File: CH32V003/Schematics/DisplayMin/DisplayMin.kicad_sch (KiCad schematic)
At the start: 9 parts

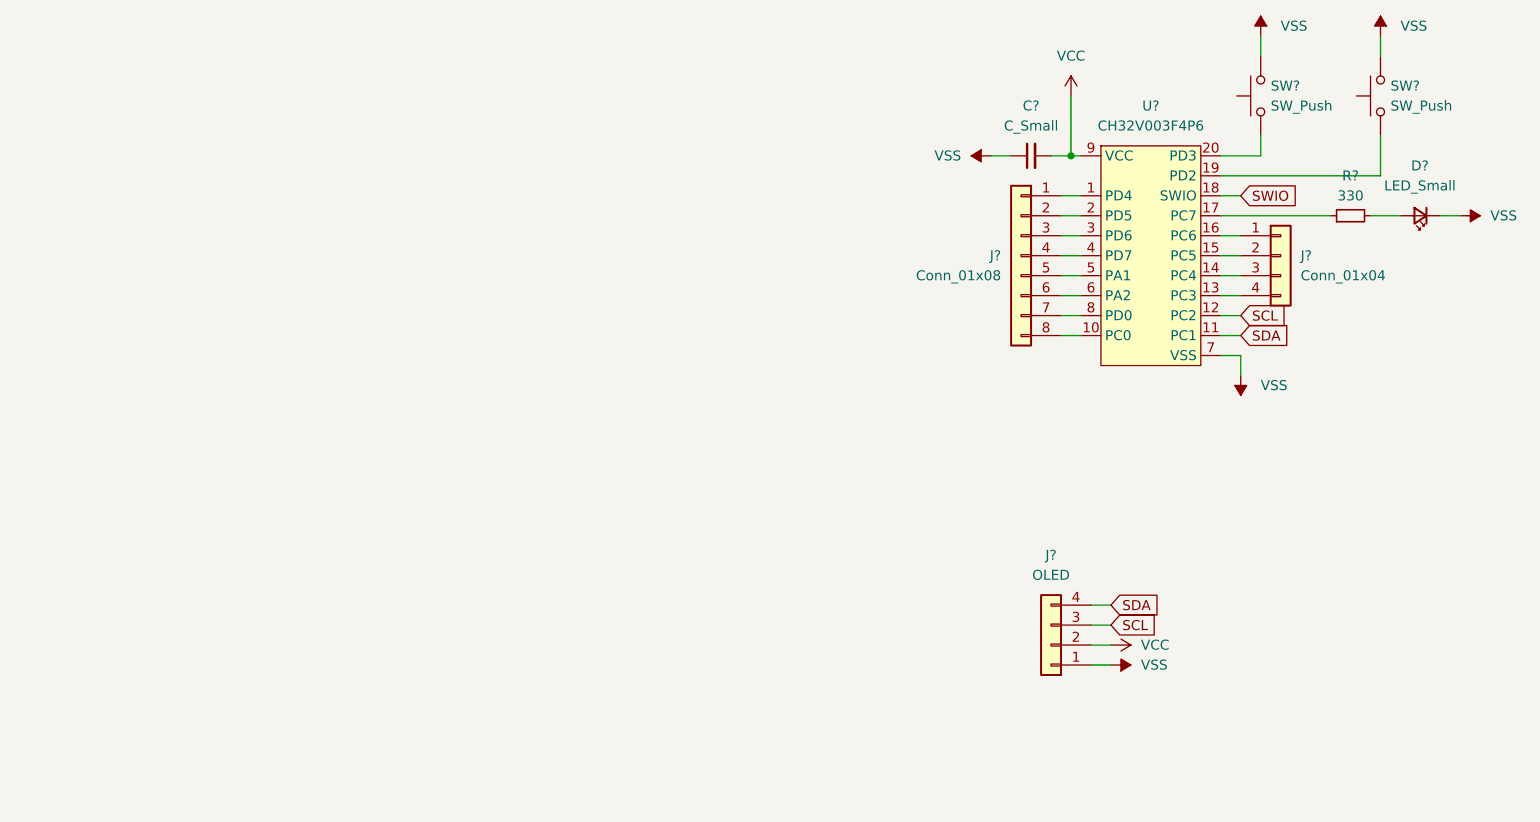
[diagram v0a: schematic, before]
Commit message: 003 dev board with display closer
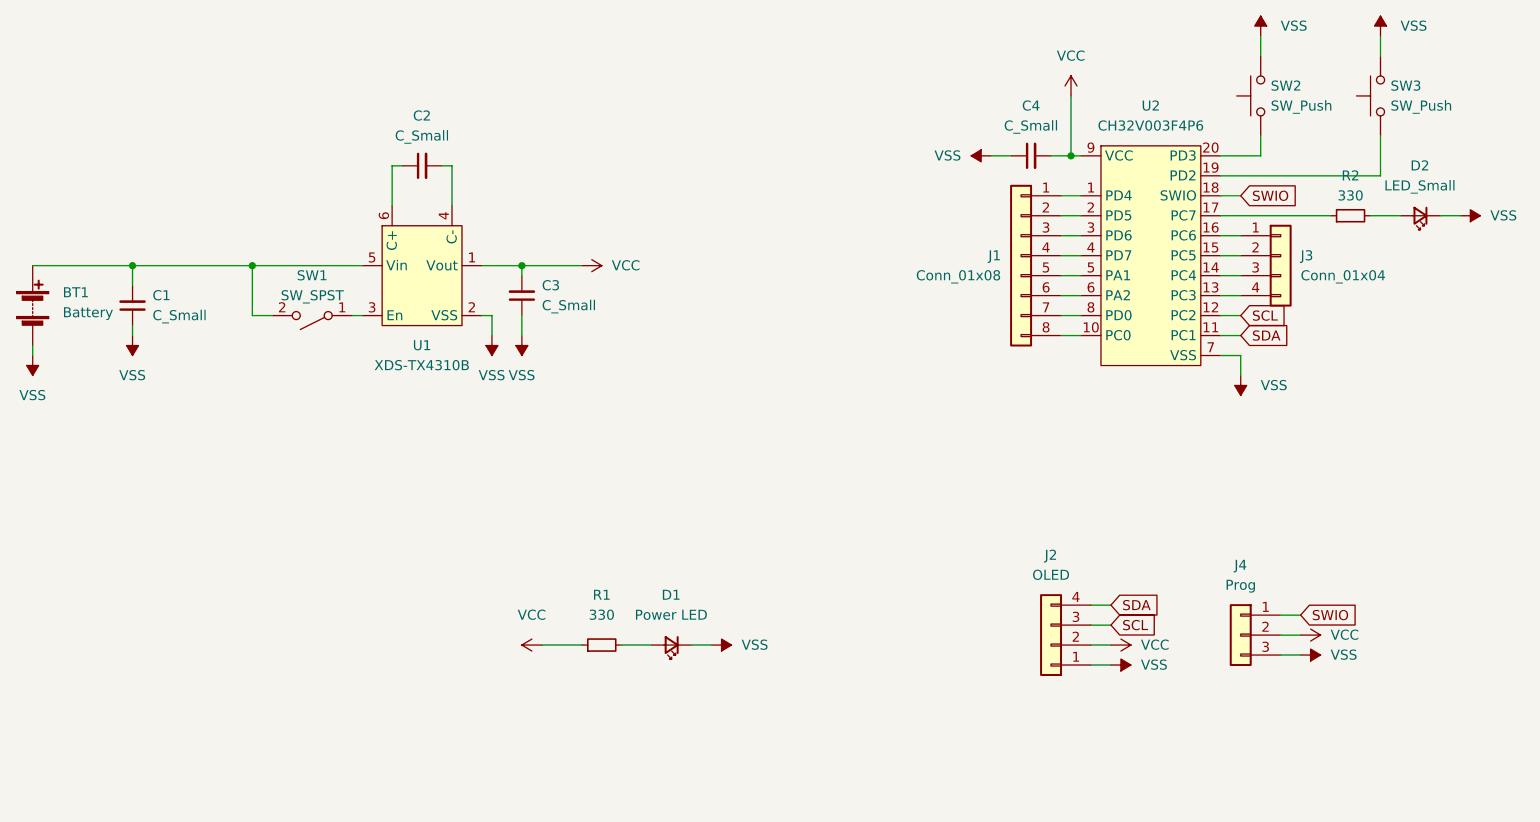
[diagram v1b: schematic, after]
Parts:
- added BT1: Battery, symbol Device:Battery
- added C1, C2, C3: C_Small, Capacitor_SMD:C_0805_2012Metric, symbol Device:C_Small
- added D1: Power LED, LED_SMD:LED_0805_2012Metric, symbol Device:LED_Small
- added J4: Prog, Connector_PinHeader_2.54mm:PinHeader_1x03_P2.54mm_Vertical, symbol Connector_Generic:Conn_01x03
- added R1: 330, Resistor_SMD:R_0805_2012Metric, symbol Device:R_Small
- added SW1: SW_SPST, symbol Switch:SW_SPST
- added U1: XDS-TX4310B, symbol WCH:XDS-TX4310B
- C4: renamed from C?; footprint (none) -> Capacitor_SMD:C_0805_2012Metric
- D2: renamed from D?; footprint (none) -> LED_SMD:LED_0805_2012Metric
- J1: renamed from J?; footprint (none) -> Connector_PinHeader_2.54mm:PinHeader_1x08_P2.54mm_Vertical
- J3: renamed from J?; footprint (none) -> Connector_PinHeader_2.54mm:PinHeader_1x04_P2.54mm_Vertical
- R2: renamed from R?; footprint (none) -> Resistor_SMD:R_0805_2012Metric
- SW2: renamed from SW?; footprint (none) -> Button_Switch_SMD:SW_SPST_EVQP0
- SW3: renamed from SW?; footprint (none) -> Button_Switch_Keyboard:SW_Cherry_MX_1.00u_PCB
- gave numbers to parts that had none: 2
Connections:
- net SWIO: now also J4.1 (Pin_1)
- net VCC: now also C3.2, J4.2 (Pin_2), R1.1, U1.1 (Vout)
- net VSS: now also BT1.2 (-), C1.1, C3.1, D1.1 (K), J4.3 (Pin_3), U1.2 (VSS)
- new net: SW1.1 (A), U1.3 (En)
- new net: C2.2, U1.4 (C-)
- new net: BT1.1 (+), C1.2, SW1.2 (B), U1.5 (Vin)
- new net: C2.1, U1.6 (C+)
- new net: D1.2 (A), R1.2

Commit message: Back to it
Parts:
- removed SW1: SW_SPST, symbol Switch:SW_SPST
- added RN1: R_Pack04, Resistor_SMD:R_Array_Concave_4x0603, symbol Device:R_Pack04
- added SW1: Power, UE-ButtonSwitch:SK-3296S_switch, symbol Switch:SW_SPDT
- BT1: footprint (none) -> UE-Battery:Keystone_1012_2AA_SMD_UE
- J2: footprint (none) -> Connector_PinHeader_2.54mm:PinHeader_1x04_P2.54mm_Vertical
- U1: footprint (none) -> Package_TO_SOT_SMD:SOT-23-6
- U2: footprint (none) -> Package_SO:SSOP-20_4.4x6.5mm_P0.65mm
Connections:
- net SCL: now also RN1.1 (R1.1)
- net SDA: now also RN1.2 (R2.1)
- net VCC: now also RN1.5 (R4.2), RN1.6 (R3.2), RN1.7 (R2.2), RN1.8 (R1.2)
- net at U1.3 (En): now also SW1.1 (A)
- net at BT1.1 (+), C1.2, U1.5 (Vin): now also SW1.2 (B)
- no-connect marks 0 -> 2
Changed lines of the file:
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@@
   (junction (at 78.74 68.58) (diameter 0) (color 0 0 0 0)
   )
+  (junction (at 135.89 130.81) (diameter 0) (color 0 0 0 0)
+  )
   (junction (at 198.12 54.61) (diameter 0) (color 0 0 0 0)
   )
+  (junction (at 135.89 133.35) (diameter 0) (color 0 0 0 0)
+  )
+  (junction (at 135.89 128.27) (diameter 0) (color 0 0 0 0)
+  )
   (junction (at 128.27 68.58) (diameter 0) (color 0 0 0 0)
   )
+  (no_connect (at 146.05 130.81))
+  (no_connect (at 146.05 128.27))
   (wire (pts (xy 66.04 68.58) (xy 78.74 68.58))
     (stroke (width 0) (type default) (color 0 0 0 0))
   )
+  (wire (pts (xy 135.89 130.81) (xy 135.89 133.35))
+    (stroke (width 0) (type default) (color 0 0 0 0))
+  )
   (wire (pts (xy 196.85 77.47) (xy 199.39 77.47))
     (stroke (width 0) (type default) (color 0 0 0 0))
@@
     (stroke (width 0) (type default) (color 0 0 0 0))
   )
+  (wire (pts (xy 135.89 133.35) (xy 135.89 135.89))
+    (stroke (width 0) (type default) (color 0 0 0 0))
+  )
   (wire (pts (xy 217.17 67.31) (xy 219.71 67.31))
     (stroke (width 0) (type default) (color 0 0 0 0))
@@
     (stroke (width 0) (type default) (color 0 0 0 0))
   )
+  (wire (pts (xy 96.52 77.47) (xy 93.98 77.47))
+    (stroke (width 0) (type default) (color 0 0 0 0))
+  )
   (wire (pts (xy 107.95 74.93) (xy 106.68 74.93))
     (stroke (width 0) (type default) (color 0 0 0 0))
@@
     (stroke (width 0) (type default) (color 0 0 0 0))
   )
+  (wire (pts (xy 146.05 133.35) (xy 149.86 133.35))
+    (stroke (width 0) (type default) (color 0 0 0 0))
+  )
   (wire (pts (xy 198.12 54.61) (xy 199.39 54.61))
     (stroke (width 0) (type default) (color 0 0 0 0))
@@
     (stroke (width 0) (type default) (color 0 0 0 0))
   )
-  (wire (pts (xy 96.52 74.93) (xy 93.98 74.93))
-    (stroke (width 0) (type default) (color 0 0 0 0))
-  )
   (wire (pts (xy 224.79 115.57) (xy 227.33 115.57))
     (stroke (width 0) (type default) (color 0 0 0 0))
@@
     (stroke (width 0) (type default) (color 0 0 0 0))
   )
+  (wire (pts (xy 130.81 128.27) (xy 135.89 128.27))
+    (stroke (width 0) (type default) (color 0 0 0 0))
+  )
   (wire (pts (xy 198.12 46.99) (xy 198.12 54.61))
     (stroke (width 0) (type default) (color 0 0 0 0))
   )
+  (wire (pts (xy 135.89 128.27) (xy 135.89 130.81))
+    (stroke (width 0) (type default) (color 0 0 0 0))
+  )
   (wire (pts (xy 195.58 54.61) (xy 198.12 54.61))
     (stroke (width 0) (type default) (color 0 0 0 0))
@@
     (stroke (width 0) (type default) (color 0 0 0 0))
   )
+  (wire (pts (xy 146.05 135.89) (xy 149.86 135.89))
+    (stroke (width 0) (type default) (color 0 0 0 0))
+  )
   (wire (pts (xy 222.25 39.37) (xy 222.25 41.91))
     (stroke (width 0) (type default) (color 0 0 0 0))
@@
     (stroke (width 0) (type default) (color 0 0 0 0))
   )
-  (wire (pts (xy 93.98 74.93) (xy 93.98 68.58))
+  (wire (pts (xy 93.98 68.58) (xy 93.98 77.47))
     (stroke (width 0) (type default) (color 0 0 0 0))
   )
@@
     )
   )
+  (global_label "SCL" (shape input) (at 149.86 135.89 0) (fields_autoplaced)
+    (effects (font (size 1.27 1.27)) (justify left))
+    (property "Intersheet References" "${INTERSHEET_REFS}" (id 0) (at 155.7807 135.8106 0)
+      (effects (font (size 1.27 1.27)) (justify left) hide)
+    )
+  )
   (global_label "SDA" (shape input) (at 203.2 111.76 0) (fields_autoplaced)
     (effects (font (size 1.27 1.27)) (justify left))
@@
     )
   )
+  (global_label "SDA" (shape input) (at 149.86 133.35 0) (fields_autoplaced)
+    (effects (font (size 1.27 1.27)) (justify left))
+    (property "Intersheet References" "${INTERSHEET_REFS}" (id 0) (at 155.8412 133.2706 0)
+      (effects (font (size 1.27 1.27)) (justify left) hide)
+    )
+  )
   (symbol (lib_id "Connector_Generic:Conn_01x03") (at 219.71 115.57 0) (mirror y) (unit 1)
     (in_bom yes) (on_board yes) (fields_autoplaced)
@@
     (pin "1")
     (pin "2")
+  )
+  (symbol (lib_id "power:VCC") (at 130.81 128.27 90) (unit 1)
+    (in_bom yes) (on_board yes) (fields_autoplaced)
+    (property "Reference" "#PWR0101" (id 0) (at 134.62 128.27 0)
+      (effects (font (size 1.27 1.27)) hide)
+    )
+    (property "Value" "VCC" (id 1) (at 129.54 124.46 90))
+    (property "Footprint" "" (id 2) (at 130.81 128.27 0)
+      (effects (font (size 1.27 1.27)) hide)
+    )
+    (property "Datasheet" "" (id 3) (at 130.81 128.27 0)
+      (effects (font (size 1.27 1.27)) hide)
+    )
+    (pin "1")
   )
   (symbol (lib_id "power:VSS") (at 219.71 82.55 180) (unit 1)
@@
     (property "Reference" "U1" (id 0) (at 115.57 78.74 0))
     (property "Value" "XDS-TX4310B" (id 1) (at 115.57 81.28 0))
-    (property "Footprint" "" (id 2) (at 115.57 71.12 0)
+    (property "Footprint" "Package_TO_SOT_SMD:SOT-23-6" (id 2) (at 115.57 71.12 0)
       (effects (font (size 1.27 1.27)) hide)
     )
@@
       (effects (font (size 1.27 1.27)) (justify left))
     )
-    (property "Footprint" "" (id 2) (at 66.04 72.136 90)
+    (property "Footprint" "UE-Battery:Keystone_1012_2AA_SMD_UE" (id 2) (at 66.04 72.136 90)
       (effects (font (size 1.27 1.27)) hide)
     )
@@
     (pin "1")
   )
-  (symbol (lib_id "Switch:SW_SPST") (at 101.6 74.93 180) (unit 1)
+  (symbol (lib_id "Switch:SW_SPDT") (at 101.6 77.47 0) (unit 1)
     (in_bom yes) (on_board yes) (fields_autoplaced)
     (property "Reference" "SW1" (id 0) (at 101.6 69.85 0))
-    (property "Value" "SW_SPST" (id 1) (at 101.6 72.39 0))
-    (property "Footprint" "" (id 2) (at 101.6 74.93 0)
-      (effects (font (size 1.27 1.27)) hide)
-    )
-    (property "Datasheet" "~" (id 3) (at 101.6 74.93 0)
-      (effects (font (size 1.27 1.27)) hide)
-    )
-    (pin "1")
-    (pin "2")
+    (property "Value" "Power" (id 1) (at 101.6 72.39 0))
+    (property "Footprint" "UE-ButtonSwitch:SK-3296S_switch" (id 2) (at 101.6 77.47 0)
+      (effects (font (size 1.27 1.27)) hide)
+    )
+    (property "Datasheet" "~" (id 3) (at 101.6 77.47 0)
+      (effects (font (size 1.27 1.27)) hide)
+    )
+    (pin "1")
+    (pin "2")
+    (pin "3")
   )
   (symbol (lib_id "Connector_Generic:Conn_01x04") (at 195.58 116.84 180) (unit 1)
@@
     (property "Reference" "J2" (id 0) (at 195.58 105.41 0))
     (property "Value" "OLED" (id 1) (at 195.58 107.95 0))
-    (property "Footprint" "" (id 2) (at 195.58 116.84 0)
+    (property "Footprint" "Connector_PinHeader_2.54mm:PinHeader_1x04_P2.54mm_Vertical" (id 2) (at 195.58 116.84 0)
       (effects (font (size 1.27 1.27)) hide)
     )
@@
     (pin "1")
   )
+  (symbol (lib_id "Device:R_Pack04") (at 140.97 130.81 90) (unit 1)
+    (in_bom yes) (on_board yes) (fields_autoplaced)
+    (property "Reference" "RN1" (id 0) (at 140.97 121.92 90))
+    (property "Value" "R_Pack04" (id 1) (at 140.97 124.46 90))
+    (property "Footprint" "Resistor_SMD:R_Array_Concave_4x0603" (id 2) (at 140.97 123.825 90)
+      (effects (font (size 1.27 1.27)) hide)
+    )
+    (property "Datasheet" "~" (id 3) (at 140.97 130.81 0)
+      (effects (font (size 1.27 1.27)) hide)
+    )
+    (pin "1")
+    (pin "2")
+    (pin "3")
+    (pin "4")
+    (pin "5")
+    (pin "6")
+    (pin "7")
+    (pin "8")
+  )
   (symbol (lib_id "Switch:SW_Push") (at 222.25 46.99 90) (unit 1)
     (in_bom yes) (on_board yes) (fields_autoplaced)
@@
     (property "Reference" "U2" (id 0) (at 208.28 48.26 0))
     (property "Value" "CH32V003F4P6" (id 1) (at 208.28 50.8 0))
-    (property "Footprint" "" (id 2) (at 208.28 58.42 0)
+    (property "Footprint" "Package_SO:SSOP-20_4.4x6.5mm_P0.65mm" (id 2) (at 208.28 58.42 0)
       (effects (font (size 1.27 1.27)) hide)
     )
@@
       (reference "#PWR017") (unit 1) (value "VSS") (footprint "")
     )
+    (path "/0adeddf0-92ec-4e8b-91a6-ada4e8d834b8"
+      (reference "#PWR0101") (unit 1) (value "VCC") (footprint "")
+    )
     (path "/4406a0de-182f-4e87-b2da-2793b3b4395a"
-      (reference "BT1") (unit 1) (value "Battery") (footprint "")
+      (reference "BT1") (unit 1) (value "Battery") (footprint "UE-Battery:Keystone_1012_2AA_SMD_UE")
     )
     (path "/c40731e3-3b44-4ce2-83b1-20b537a1c146"
@@
     )
     (path "/79fcb49f-fb5a-469d-b38b-283bd5d44bf2"
-      (reference "J2") (unit 1) (value "OLED") (footprint "")
+      (reference "J2") (unit 1) (value "OLED") (footprint "Connector_PinHeader_2.54mm:PinHeader_1x04_P2.54mm_Vertical")
     )
     (path "/7bb2e183-1e9f-4da1-bba8-8d4a4fb9b86f"
@@
       (reference "R2") (unit 1) (value "330") (footprint "Resistor_SMD:R_0805_2012Metric")
     )
-    (path "/71ceea23-a1c8-4900-8c7a-6bd2f76f9260"
-      (reference "SW1") (unit 1) (value "SW_SPST") (footprint "")
+    (path "/dd9b4fb8-c3e7-49ab-9f8f-506c7a657dcf"
+      (reference "RN1") (unit 1) (value "R_Pack04") (footprint "Resistor_SMD:R_Array_Concave_4x0603")
+    )
+    (path "/713f8fa4-8720-4b51-813f-9aa328f2832b"
+      (reference "SW1") (unit 1) (value "Power") (footprint "UE-ButtonSwitch:SK-3296S_switch")
     )
     (path "/f0396047-ce8e-4c52-a5f0-f630979479b9"
@@
     )
     (path "/3117a5fe-8bce-4afa-b826-6ce9a73f9130"
-      (reference "U1") (unit 1) (value "XDS-TX4310B") (footprint "")
+      (reference "U1") (unit 1) (value "XDS-TX4310B") (footprint "Package_TO_SOT_SMD:SOT-23-6")
     )
     (path "/fd27eac8-4d59-48ea-8ab7-e4ee68ec2c4e"
-      (reference "U2") (unit 1) (value "CH32V003F4P6") (footprint "")
-    )
-  )
+      (reference "U2") (unit 1) (value "CH32V003F4P6") (footprint "Package_SO:SSOP-20_4.4x6.5mm_P0.65mm")
+    )
+  )
